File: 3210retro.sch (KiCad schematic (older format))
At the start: 20 parts, among them P101 USB_OTG, P103 LIPO, P104 DC, P105 EAR, P106 SPEAKER, P107 HEADPHONE, P108 RUMBLE, X101 ANT_GPS, X102 ANT_GSM

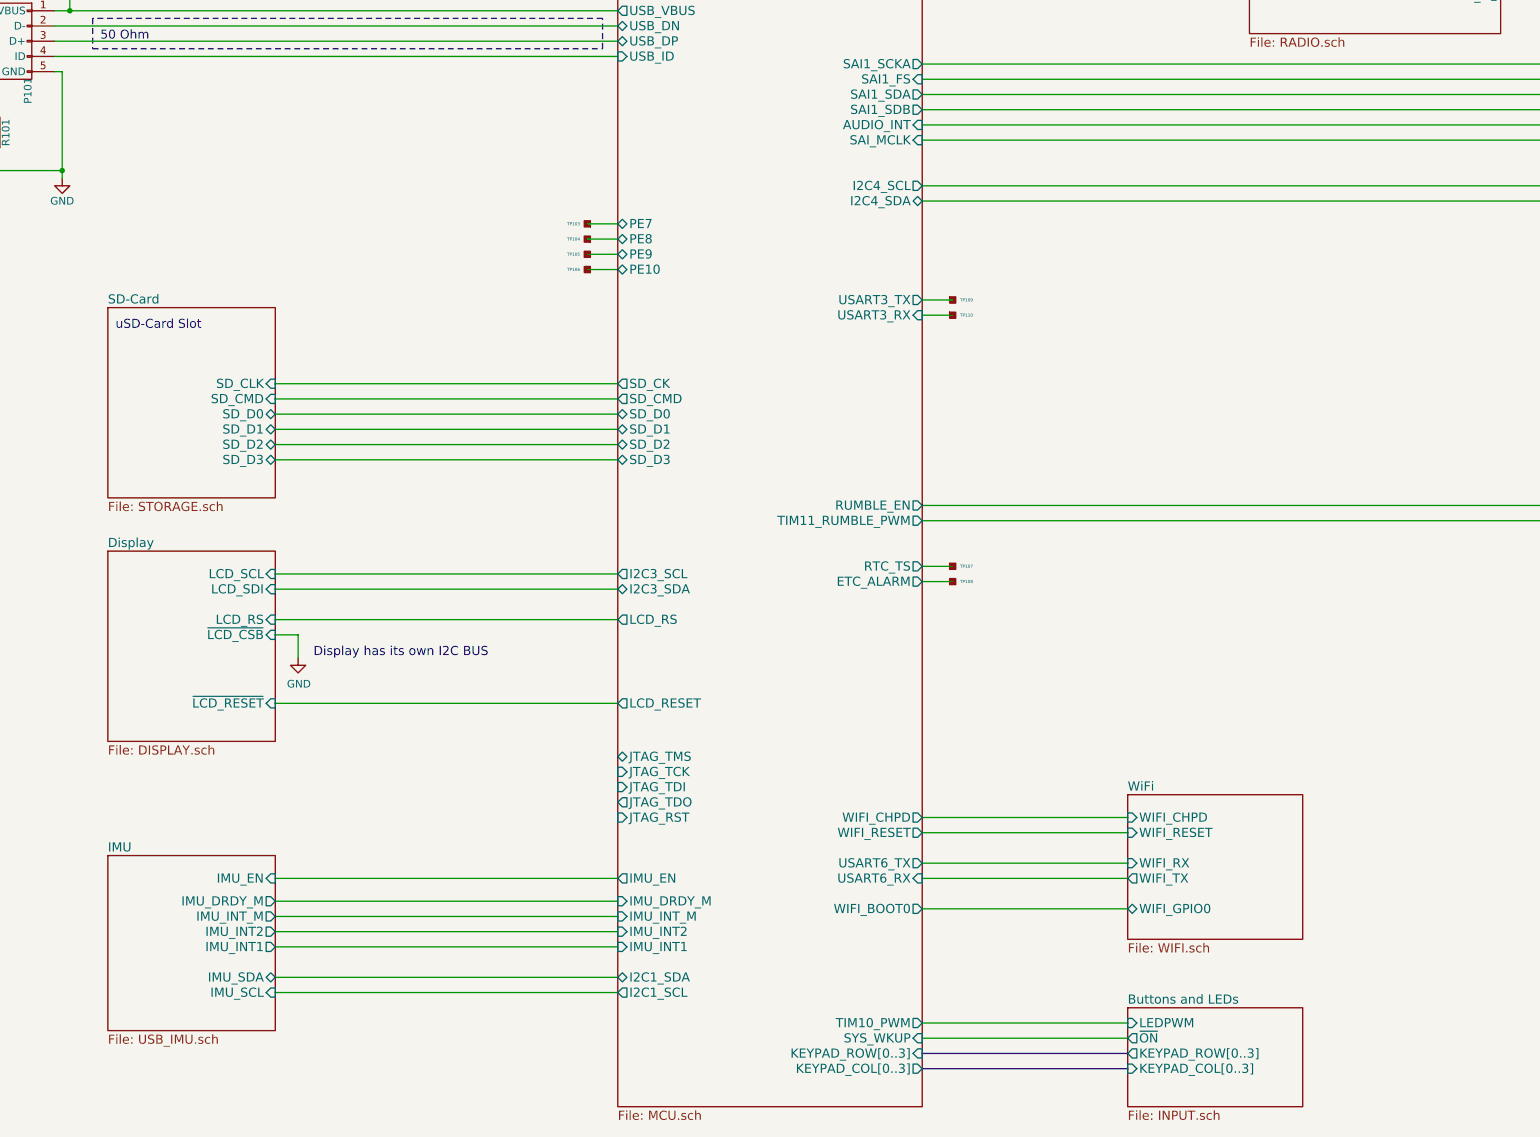
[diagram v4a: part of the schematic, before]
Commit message: fix for several signals
* some signals where not routed out to the top sheet.
* I2C signals where not connected.
* moved imu subsheet to the other side of the mcu sheet to
  share I2C bus with audio
* changed footprint of crystals to crystals I have
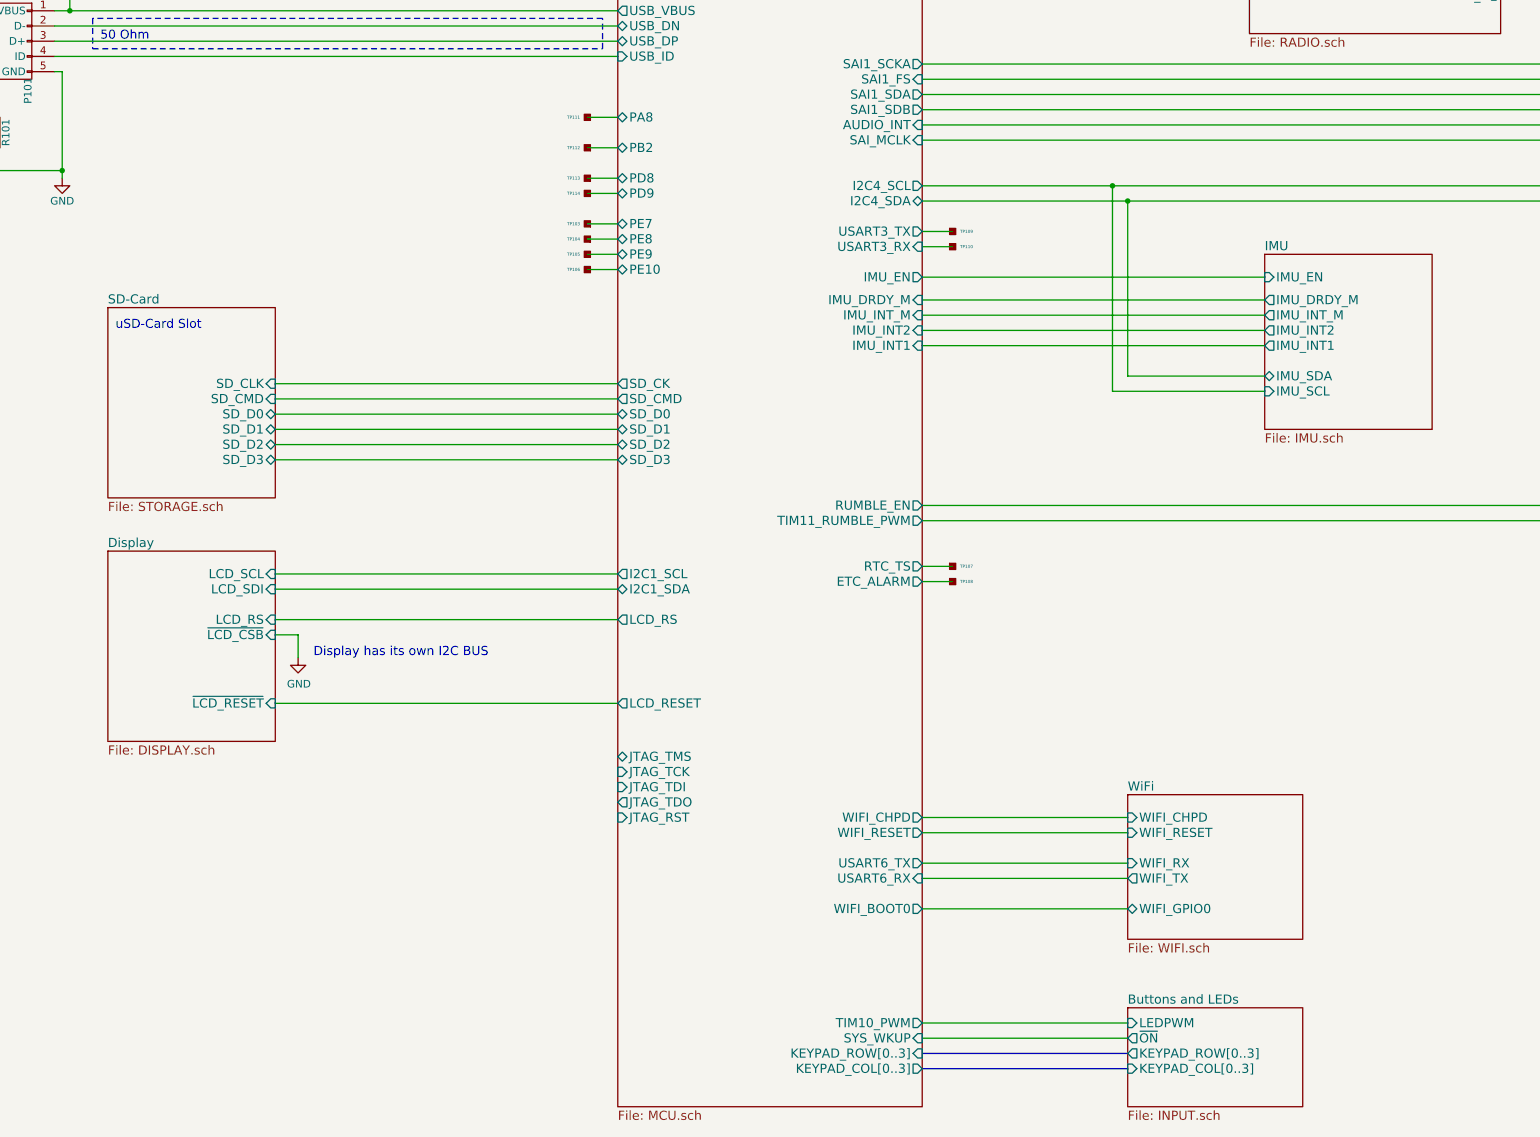
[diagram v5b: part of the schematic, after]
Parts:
- added TP111, TP112, TP113, TP114: TP, NokiaRetroFit:TP, symbol TP
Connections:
- wire segments 93 -> 99
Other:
- moved on the sheet: TP109, TP110
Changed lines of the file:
@@
 F15 "ADC2" I L 5650 2450 60
 F16 "ADC3" I L 5650 2250 60
-F17 "I2C3_SCL" O L 5650 7300 60
-F18 "USART1_TX" O R 7650 3350 60
-F19 "USART1_RX" I R 7650 3250 60
-F20 "JTAG_TMS" B L 5650 8500 60
-F21 "JTAG_TCK" I L 5650 8600 60
-F22 "JTAG_TDI" I L 5650 8700 60
-F23 "JTAG_TDO" O L 5650 8800 60
-F24 "I2C1_SCL" O L 5650 10050 60
-F25 "USART3_TX" O R 7650 5500 60
-F26 "USART3_RX" I R 7650 5600 60
-F27 "USB_ID" I L 5650 3900 60
-F28 "USB_VBUS" O L 5650 3600 60
-F29 "USB_DP" B L 5650 3800 60
-F30 "RTC_TS" O R 7650 7250 60
-F31 "USART6_TX" O R 7650 9200 60
-F32 "USART6_RX" I R 7650 9300 60
-F33 "SD_D0" B L 5650 6250 60
-F34 "I2C3_SDA" B L 5650 7400 60
-F35 "SD_CK" O L 5650 6050 60
-F36 "ETC_ALARM" O R 7650 7350 60
-F37 "VBAT" I L 5650 1700 60
-F38 "TIM10_PWM" O R 7650 10250 60
-F39 "JTAG_RST" I L 5650 8900 60
-F40 "I2C1_SDA" B L 5650 9950 60
-F41 "LCD_RS" O L 5650 7600 60
-F42 "LCD_RESET" O L 5650 8150 60
-F43 "~CHARGING" I L 5650 2750 60
-F44 "IMU_DRDY_M" I L 5650 9450 60
-F45 "IMU_INT_M" I L 5650 9550 60
-F46 "IMU_INT2" I L 5650 9650 60
-F47 "IMU_INT1" I L 5650 9750 60
-F48 "IMU_EN" O L 5650 9300 60
-F49 "UART8_CTS" O R 7650 2550 60
-F50 "UART8_RTS" I R 7650 2450 60
-F51 "RADIO_ACTIVE" O R 7650 2250 60
-F52 "RADIO_RST" O R 7650 2050 60
-F53 "WIFI_CHPD" O R 7650 8900 60
-F54 "WIFI_RESET" O R 7650 9000 60
-F55 "WIFI_BOOT0" O R 7650 9500 60
-F56 "RADIO_ON" O R 7650 2150 60
-F57 "NVCC_3V3_EN" O L 5650 2050 60
-F58 "U3V3_PG" I L 5650 2850 60
-F59 "SAI1_SCKA" O R 7650 3950 60
-F60 "SAI1_SDA" O R 7650 4150 60
-F61 "SAI1_SDB" O R 7650 4250 60
-F62 "AUDIO_INT" I R 7650 4350 60
-F63 "RUMBLE_EN" O R 7650 6850 60
-F64 "TIM11_RUMBLE_PWM" O R 7650 6950 60
-F65 "SD_D1" B L 5650 6350 60
-F66 "SD_D2" B L 5650 6450 60
-F67 "SD_D3" B L 5650 6550 60
-F68 "PE7" B L 5650 5000 60
-F69 "PE8" B L 5650 5100 60
-F70 "PE9" B L 5650 5200 60
-F71 "PE10" B L 5650 5300 60
-F72 "USB_DN" B L 5650 3700 60
+F17 "USART1_TX" O R 7650 3350 60
+F18 "USART1_RX" I R 7650 3250 60
+F19 "JTAG_TMS" B L 5650 8500 60
+F20 "JTAG_TCK" I L 5650 8600 60
+F21 "JTAG_TDI" I L 5650 8700 60
+F22 "JTAG_TDO" O L 5650 8800 60
+F23 "I2C1_SCL" O L 5650 7300 60
+F24 "USART3_TX" O R 7650 5050 60
+F25 "USART3_RX" I R 7650 5150 60
+F26 "USB_ID" I L 5650 3900 60
+F27 "USB_VBUS" O L 5650 3600 60
+F28 "USB_DP" B L 5650 3800 60
+F29 "RTC_TS" O R 7650 7250 60
+F30 "USART6_TX" O R 7650 9200 60
+F31 "USART6_RX" I R 7650 9300 60
+F32 "SD_D0" B L 5650 6250 60
+F33 "SD_CK" O L 5650 6050 60
+F34 "ETC_ALARM" O R 7650 7350 60
+F35 "VBAT" I L 5650 1700 60
+F36 "TIM10_PWM" O R 7650 10250 60
+F37 "JTAG_RST" I L 5650 8900 60
+F38 "I2C1_SDA" B L 5650 7400 60
+F39 "LCD_RS" O L 5650 7600 60
+F40 "LCD_RESET" O L 5650 8150 60
+F41 "~CHARGING" I L 5650 2750 60
+F42 "IMU_DRDY_M" I R 7650 5500 60
+F43 "IMU_INT_M" I R 7650 5600 60
+F44 "IMU_INT2" I R 7650 5700 60
+F45 "IMU_INT1" I R 7650 5800 60
+F46 "IMU_EN" O R 7650 5350 60
+F47 "UART8_CTS" O R 7650 2550 60
+F48 "UART8_RTS" I R 7650 2450 60
+F49 "RADIO_ACTIVE" O R 7650 2250 60
+F50 "RADIO_RST" O R 7650 2050 60
+F51 "WIFI_CHPD" O R 7650 8900 60
+F52 "WIFI_RESET" O R 7650 9000 60
+F53 "WIFI_BOOT0" O R 7650 9500 60
+F54 "RADIO_ON" O R 7650 2150 60
+F55 "NVCC_3V3_EN" O L 5650 2050 60
+F56 "U3V3_PG" I L 5650 2850 60
+F57 "SAI1_SCKA" O R 7650 3950 60
+F58 "SAI1_SDA" O R 7650 4150 60
+F59 "SAI1_SDB" O R 7650 4250 60
+F60 "AUDIO_INT" I R 7650 4350 60
+F61 "RUMBLE_EN" O R 7650 6850 60
+F62 "TIM11_RUMBLE_PWM" O R 7650 6950 60
+F63 "SD_D1" B L 5650 6350 60
+F64 "SD_D2" B L 5650 6450 60
+F65 "SD_D3" B L 5650 6550 60
+F66 "PE7" B L 5650 5000 60
+F67 "PE8" B L 5650 5100 60
+F68 "PE9" B L 5650 5200 60
+F69 "PE10" B L 5650 5300 60
+F70 "USB_DN" B L 5650 3700 60
+F71 "PD8" B L 5650 4700 60
+F72 "PD9" B L 5650 4800 60
+F73 "PB2" B L 5650 4500 60
+F74 "PA8" B L 5650 4300 60
 $EndSheet
 $Comp
@@
 Connection ~ 2050 3600
 Wire Wire Line
-	3400 9750 5650 9750
-Wire Wire Line
-	3400 9650 5650 9650
-Wire Wire Line
-	3400 9550 5650 9550
-Wire Wire Line
-	3400 9450 5650 9450
-Wire Wire Line
-	3400 9300 5650 9300
-Wire Wire Line
-	3400 10050 5650 10050
-Wire Wire Line
-	3400 9950 5650 9950
+	9900 5800 7650 5800
+Wire Wire Line
+	9900 5700 7650 5700
+Wire Wire Line
+	9900 5600 7650 5600
+Wire Wire Line
+	9900 5500 7650 5500
+Wire Wire Line
+	9900 5350 7650 5350
+Wire Wire Line
+	9900 6100 8900 6100
+Wire Wire Line
+	9900 6000 9000 6000
 $Sheet
-S 2300 9150 1100 1150
+S 9900 5200 1100 1150
 U 59B32194
 F0 "IMU" 60
-F1 "USB_IMU.sch" 60
-F2 "IMU_SDA" B R 3400 9950 60
-F3 "IMU_SCL" I R 3400 10050 60
-F4 "IMU_INT1" O R 3400 9750 60
-F5 "IMU_INT2" O R 3400 9650 60
-F6 "IMU_DRDY_M" O R 3400 9450 60
-F7 "IMU_INT_M" O R 3400 9550 60
-F8 "IMU_EN" I R 3400 9300 60
+F1 "IMU.sch" 60
+F2 "IMU_SDA" B L 9900 6000 60
+F3 "IMU_SCL" I L 9900 6100 60
+F4 "IMU_INT1" O L 9900 5800 60
+F5 "IMU_INT2" O L 9900 5700 60
+F6 "IMU_DRDY_M" O L 9900 5500 60
+F7 "IMU_INT_M" O L 9900 5600 60
+F8 "IMU_EN" I L 9900 5350 60
 $EndSheet
 Wire Wire Line
@@
 L TP TP110
 U 1 1 59B5F8E6
-P 7850 5600
-F 0 "TP110" H 7898 5600 20  0000 L CNN
-F 1 "TP" H 7850 5550 60  0001 C CNN
-F 2 "NokiaRetroFit:TP" H 7850 5600 60  0001 C CNN
-F 3 "" H 7850 5600 60  0000 C CNN
-	1    7850 5600
+P 7850 5150
+F 0 "TP110" H 7898 5150 20  0000 L CNN
+F 1 "TP" H 7850 5100 60  0001 C CNN
+F 2 "NokiaRetroFit:TP" H 7850 5150 60  0001 C CNN
+F 3 "" H 7850 5150 60  0000 C CNN
+	1    7850 5150
 	1    0    0    -1
 $EndComp
@@
 L TP TP109
 U 1 1 59B5F8EC
-P 7850 5500
-F 0 "TP109" H 7898 5500 20  0000 L CNN
-F 1 "TP" H 7850 5450 60  0001 C CNN
-F 2 "NokiaRetroFit:TP" H 7850 5500 60  0001 C CNN
-F 3 "" H 7850 5500 60  0000 C CNN
-	1    7850 5500
-	1    0    0    -1
-$EndComp
-Wire Wire Line
-	7850 5500 7650 5500
-Wire Wire Line
-	7650 5600 7850 5600
+P 7850 5050
+F 0 "TP109" H 7898 5050 20  0000 L CNN
+F 1 "TP" H 7850 5000 60  0001 C CNN
+F 2 "NokiaRetroFit:TP" H 7850 5050 60  0001 C CNN
+F 3 "" H 7850 5050 60  0000 C CNN
+	1    7850 5050
+	1    0    0    -1
+$EndComp
+Wire Wire Line
+	7850 5050 7650 5050
+Wire Wire Line
+	7650 5150 7850 5150
 $Comp
 L GNDA #PWR01
@@
 Wire Wire Line
 	3400 6550 5650 6550
+Wire Wire Line
+	8900 6100 8900 4750
+Connection ~ 8900 4750
+Wire Wire Line
+	9000 6000 9000 4850
+Connection ~ 9000 4850
+$Comp
+L TP TP114
+U 1 1 59BBF2A2
+P 5450 4800
+F 0 "TP114" H 5498 4800 20  0000 L CNN
+F 1 "TP" H 5450 4750 60  0001 C CNN
+F 2 "NokiaRetroFit:TP" H 5450 4800 60  0001 C CNN
+F 3 "" H 5450 4800 60  0000 C CNN
+	1    5450 4800
+	-1   0    0    1
+$EndComp
+$Comp
+L TP TP113
+U 1 1 59BBF2A8
+P 5450 4700
+F 0 "TP113" H 5498 4700 20  0000 L CNN
+F 1 "TP" H 5450 4650 60  0001 C CNN
+F 2 "NokiaRetroFit:TP" H 5450 4700 60  0001 C CNN
+F 3 "" H 5450 4700 60  0000 C CNN
+	1    5450 4700
+	-1   0    0    1
+$EndComp
+$Comp
+L TP TP111
+U 1 1 59BBF2AE
+P 5450 4300
+F 0 "TP111" H 5498 4300 20  0000 L CNN
+F 1 "TP" H 5450 4250 60  0001 C CNN
+F 2 "NokiaRetroFit:TP" H 5450 4300 60  0001 C CNN
+F 3 "" H 5450 4300 60  0000 C CNN
+	1    5450 4300
+	-1   0    0    1
+$EndComp
+$Comp
+L TP TP112
+U 1 1 59BBF2B4
+P 5450 4500
+F 0 "TP112" H 5498 4500 20  0000 L CNN
+F 1 "TP" H 5450 4450 60  0001 C CNN
+F 2 "NokiaRetroFit:TP" H 5450 4500 60  0001 C CNN
+F 3 "" H 5450 4500 60  0000 C CNN
+	1    5450 4500
+	-1   0    0    1
+$EndComp
+Wire Wire Line
+	5650 4500 5450 4500
+Wire Wire Line
+	5450 4300 5650 4300
+Wire Wire Line
+	5650 4700 5450 4700
+Wire Wire Line
+	5450 4800 5650 4800
 $EndSCHEMATC

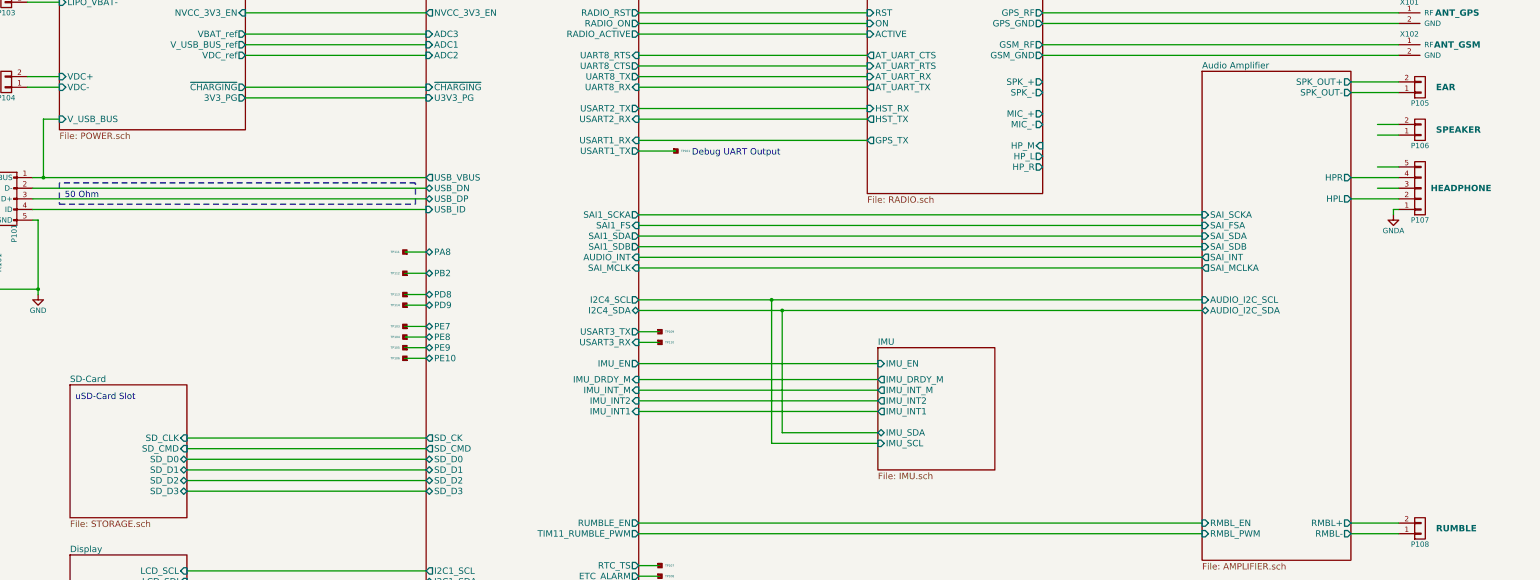
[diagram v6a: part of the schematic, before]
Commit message: changed sound subsystem
rerouted all the changed tracks
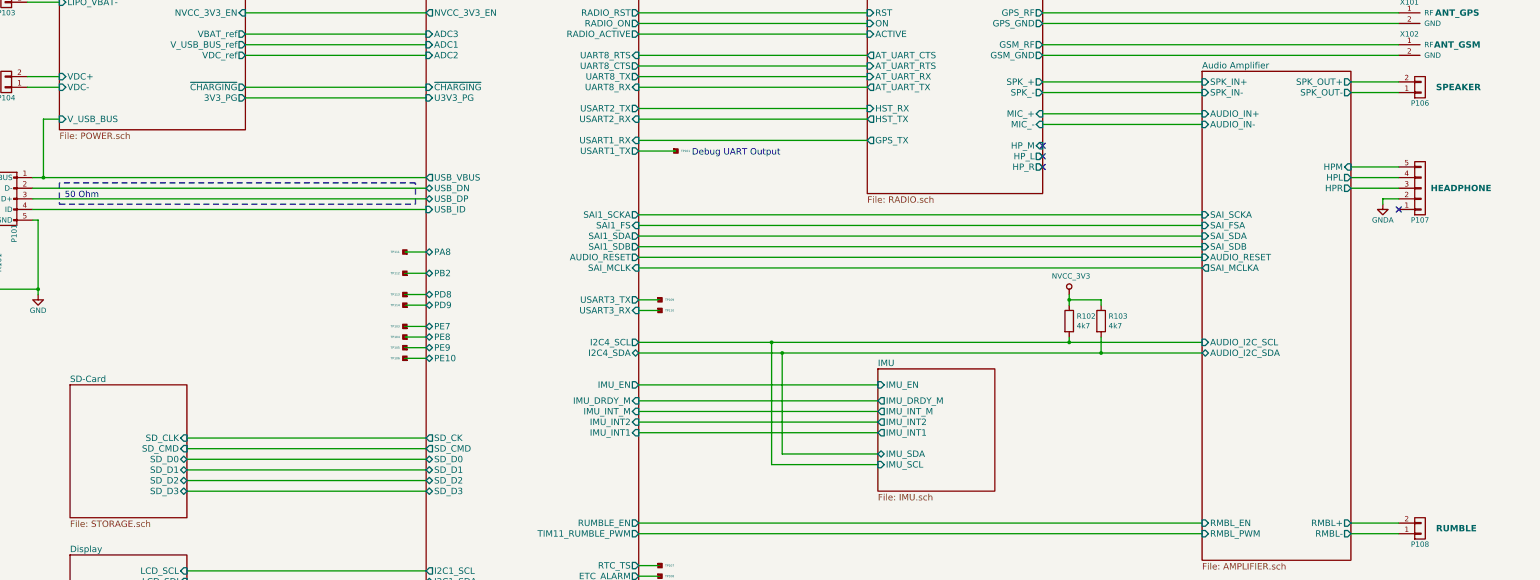
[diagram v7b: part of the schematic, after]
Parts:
- removed P105: EAR, NokiaRetroFit:SolderWirePad_2x_0,8, symbol CONN_01X02
- added R102, R103: 4k7, Resistors_SMD:R_0402_NoSilk, symbol R
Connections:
- net labels added: NVCC_3V3
- wire segments 99 -> 105
- no-connect marks 0 -> 4
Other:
- note removed: "uSD-Card Slot"
- moved on the sheet: P106, TP109, TP110
